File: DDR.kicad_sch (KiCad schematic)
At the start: 12 parts, among them U1 rv1126/rv1109, U2 Micron DDR4 MT40A512M16TB

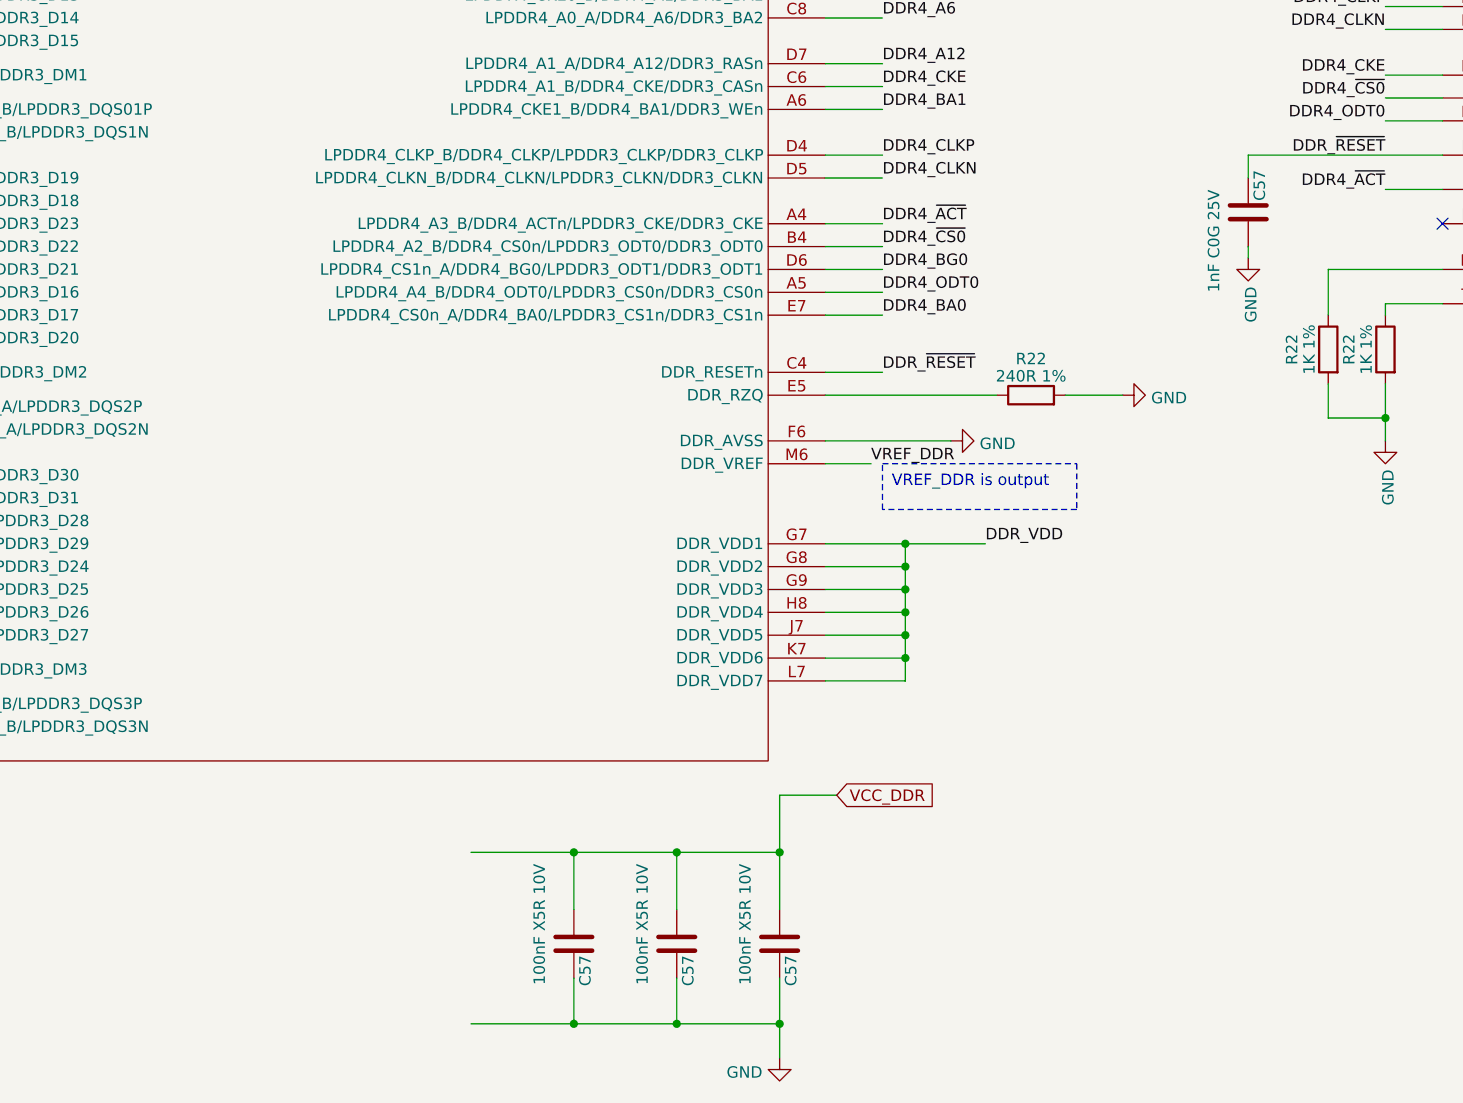
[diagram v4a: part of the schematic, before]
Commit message: updated Capacitors
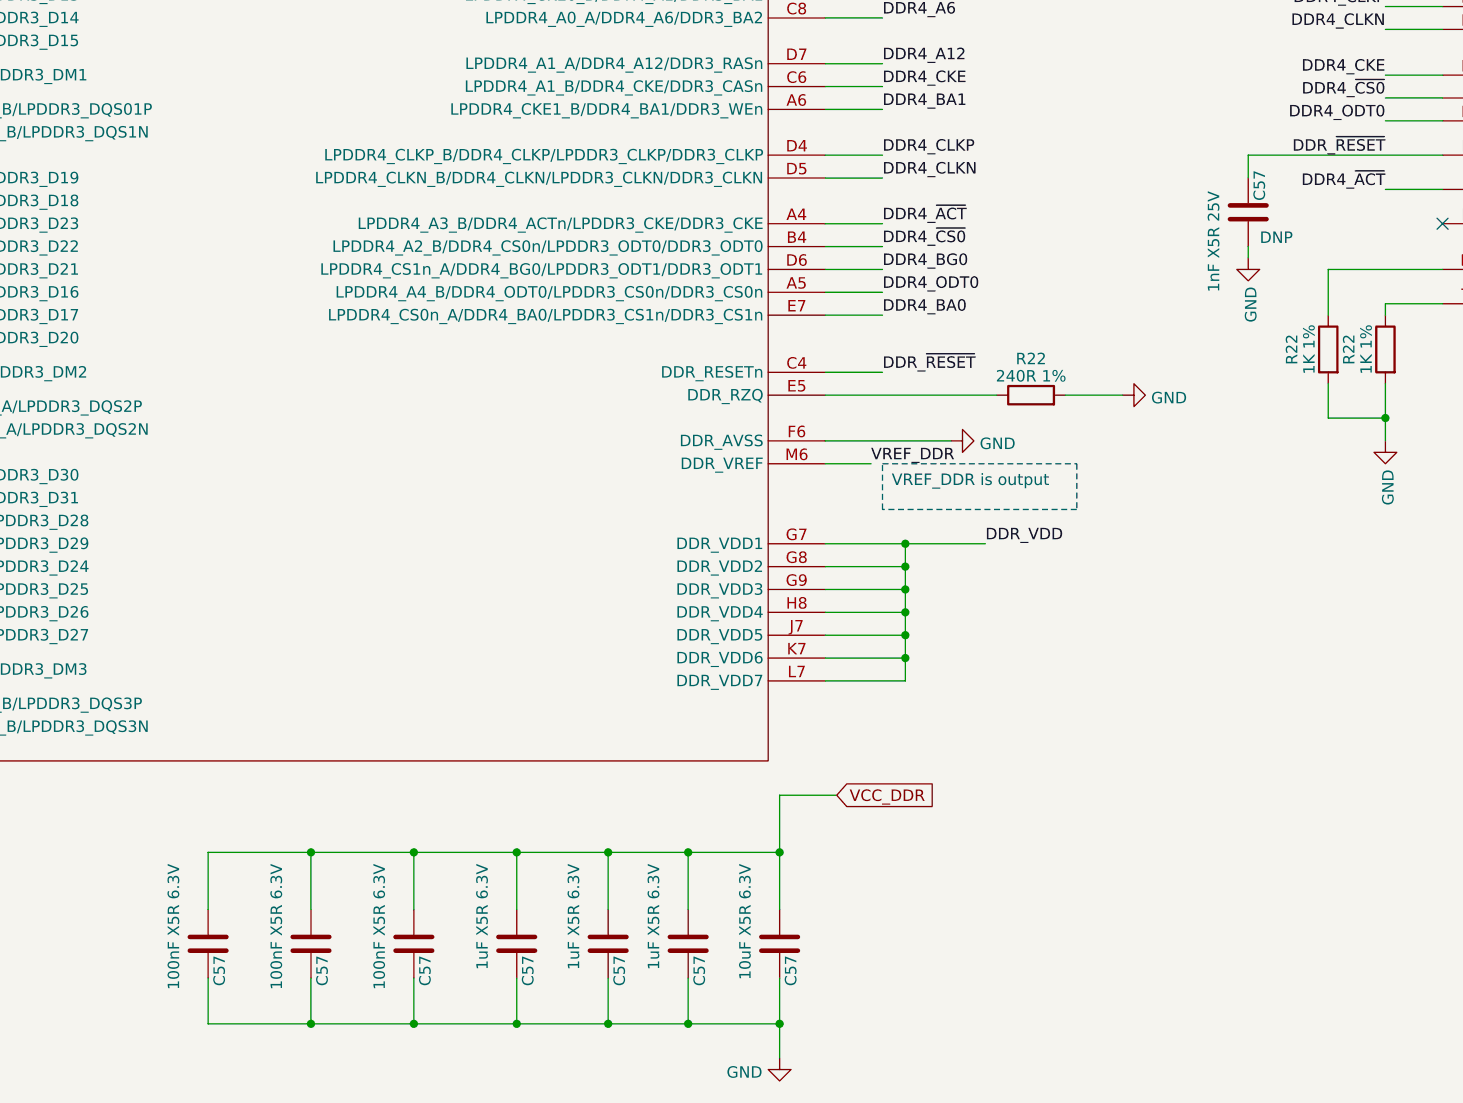
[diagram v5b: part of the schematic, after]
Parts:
- added C57 (x3): 1uF X5R 6.3V, Capacitor_SMD:C_0201_0603Metric, symbol Device:C
- added C57: 10uF X5R 6.3V, Capacitor_SMD:C_0603_1608Metric, symbol Device:C
- C57: footprint Capacitor_SMD:C_0402_1005Metric -> Capacitor_SMD:C_0201_0603Metric; now left out of the parts list
- C57: value 1nF C0G 25V -> 1nF X5R 25V; footprint Capacitor_SMD:C_0402_1005Metric -> Capacitor_SMD:C_0201_0603Metric; LCSC (none) -> C161477; Model (none) -> GRM033R61E102KA01D; Vendor (none) -> muRata(村田); now left out of the parts list
- C57: value 100nF X5R 10V -> 100nF X5R 6.3V; footprint Capacitor_SMD:C_0402_1005Metric -> Capacitor_SMD:C_0201_0603Metric; LCSC (none) -> C76934; Model (none) -> GRM033R61A104KE15D; Vendor (none) -> muRata(村田)
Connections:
- net GND: now also C57.1, C57.1, C57.1, C57.1
- net VCC_DDR: now also C57.2, C57.2, C57.2, C57.2
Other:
- moved on the sheet: C57

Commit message: updated LCSC selection of capacitors
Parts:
- C57: footprint Capacitor_SMD:C_0603_1608Metric -> Capacitor_SMD:C_0402_1005Metric; LCSC (none) -> C77000; Model (none) -> GRM155R61A106ME44D; Vendor (none) -> muRata(村田)
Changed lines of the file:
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@@
       (effects (font (size 1.27 1.27)) (justify left))
     )
-    (property "Footprint" "Capacitor_SMD:C_0603_1608Metric" (at 154.6352 176.53 0)
+    (property "Footprint" "Capacitor_SMD:C_0402_1005Metric" (at 154.6352 176.53 0)
       (effects (font (size 1.27 1.27)) hide)
     )
@@
       (effects (font (size 1.27 1.27)) hide)
     )
+    (property "Description" "容值: 10uF 精度: ±20% 额定电压: 10V 材质(温度系数): X5R 材质:X5R" (at 153.67 180.34 0)
+      (effects (font (size 1.27 1.27)) hide)
+    )
+    (property "LCSC" "C77000" (at 153.67 180.34 0)
+      (effects (font (size 1.27 1.27)) hide)
+    )
+    (property "Model" "GRM155R61A106ME44D" (at 153.67 180.34 0)
+      (effects (font (size 1.27 1.27)) hide)
+    )
+    (property "Vendor" "muRata(村田)" (at 153.67 180.34 0)
+      (effects (font (size 1.27 1.27)) hide)
+    )

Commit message: updated DDR_VDD
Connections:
- net DDR_VDD is gone; now on net VCC_DDR: U1.G7 (DDR_VDD1), U1.G8 (DDR_VDD2), U1.G9 (DDR_VDD3), U1.H8 (DDR_VDD4), U1.J7 (DDR_VDD5), U1.K7 (DDR_VDD6), U1.L7 (DDR_VDD7)
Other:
- moved on the sheet: C57, R22

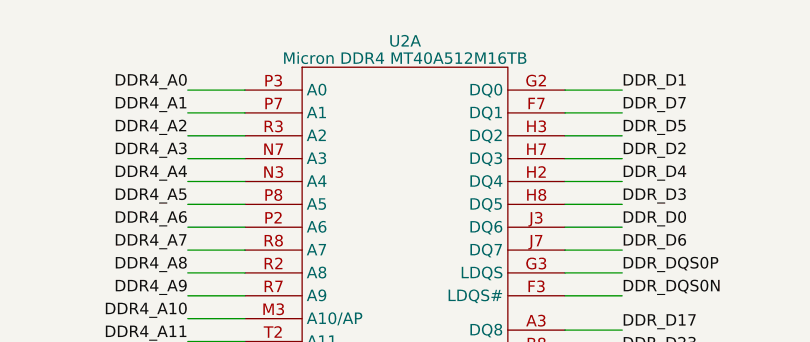
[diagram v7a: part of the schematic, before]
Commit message: layout SoC Power and DDR capacitors
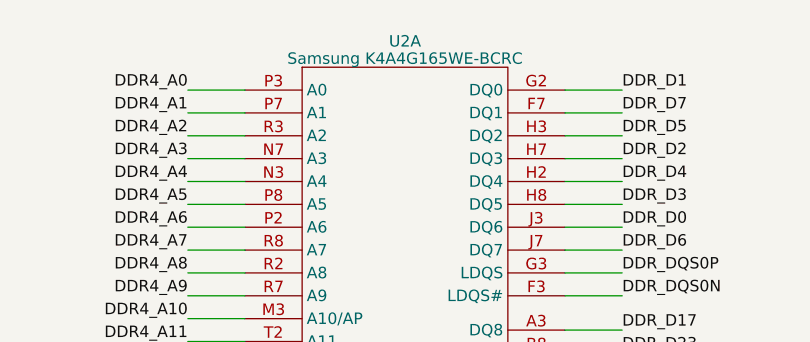
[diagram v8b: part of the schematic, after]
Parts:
- C57: LCSC C76934 -> C76928; Model GRM033R61A104KE15D -> GRM033R60J104KE19D
- C57: footprint Capacitor_SMD:C_0201_0603Metric -> Capacitor_SMD:C_0402_1005Metric; LCSC C76929 -> C15684; Model GRM033R60J105KEA2D -> GRM155R60J105KE19D
- U2: value Micron DDR4 MT40A512M16TB -> Samsung K4A4G165WE-BCRC; footprint (none) -> Package_BGA:Micron_FBGA-96_9x14mm_Layout9x16_P0.8mm; LCSC (none) -> C2803250; Model (none) -> K4A4G165WE-BCRC; Vendor (none) -> SAMSUNG(三星半导体)
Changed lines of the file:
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@@
       (effects (font (size 1.27 1.27)))
     )
-    (property "Value" "Micron DDR4 MT40A512M16TB" (at 245.11 25.7081 0)
-      (effects (font (size 1.27 1.27)))
-    )
-    (property "Footprint" "" (at 245.11 64.77 0)
+    (property "Value" "Samsung K4A4G165WE-BCRC" (at 245.11 25.7081 0)
+      (effects (font (size 1.27 1.27)))
+    )
+    (property "Footprint" "Package_BGA:Micron_FBGA-96_9x14mm_Layout9x16_P0.8mm" (at 245.11 64.77 0)
       (effects (font (size 1.27 1.27)) hide)
     )
     (property "Datasheet" "" (at 245.11 64.77 0)
+      (effects (font (size 1.27 1.27)) hide)
+    )
+    (property "Description" "存储器构架(格式): SDRAM DDR4 时钟频率(fc): 1200MHz 存储容量: 4Gbit 工作电压: 1.14V~1.26V 工作电" (at 245.11 64.77 0)
+      (effects (font (size 1.27 1.27)) hide)
+    )
+    (property "LCSC" "C2803250" (at 245.11 64.77 0)
+      (effects (font (size 1.27 1.27)) hide)
+    )
+    (property "Model" "K4A4G165WE-BCRC" (at 245.11 64.77 0)
+      (effects (font (size 1.27 1.27)) hide)
+    )
+    (property "Vendor" "SAMSUNG(三星半导体)" (at 245.11 64.77 0)
       (effects (font (size 1.27 1.27)) hide)
     )
@@
       (effects (font (size 1.27 1.27)) hide)
     )
-    (property "Description" "容值: 100nF 精度: ±10% 额定电压: 10V 材质(温度系数): X5R 材质:X5R" (at 138.43 180.34 0)
-      (effects (font (size 1.27 1.27)) hide)
-    )
-    (property "LCSC" "C76934" (at 138.43 180.34 0)
-      (effects (font (size 1.27 1.27)) hide)
-    )
-    (property "Model" "GRM033R61A104KE15D" (at 138.43 180.34 0)
+    (property "Description" "容值: 100nF 精度: ±10% 额定电压: 6.3V 材质(温度系数): X5R 材质:X5R" (at 138.43 180.34 0)
+      (effects (font (size 1.27 1.27)) hide)
+    )
+    (property "LCSC" "C76928" (at 138.43 180.34 0)
+      (effects (font (size 1.27 1.27)) hide)
+    )
+    (property "Model" "GRM033R60J104KE19D" (at 138.43 180.34 0)
       (effects (font (size 1.27 1.27)) hide)
     )
@@
       (effects (font (size 1.27 1.27)) (justify left))
     )
-    (property "Footprint" "Capacitor_SMD:C_0201_0603Metric" (at 115.8748 176.53 0)
+    (property "Footprint" "Capacitor_SMD:C_0402_1005Metric" (at 115.8748 176.53 0)
       (effects (font (size 1.27 1.27)) hide)
     )
@@
       (effects (font (size 1.27 1.27)) hide)
     )
-    (property "LCSC" "C76929" (at 116.84 180.34 0)
-      (effects (font (size 1.27 1.27)) hide)
-    )
-    (property "Model" "GRM033R60J105KEA2D" (at 116.84 180.34 0)
+    (property "LCSC" "C15684" (at 116.84 180.34 0)
+      (effects (font (size 1.27 1.27)) hide)
+    )
+    (property "Model" "GRM155R60J105KE19D" (at 116.84 180.34 0)
       (effects (font (size 1.27 1.27)) hide)
     )
@@
       (effects (font (size 1.27 1.27)) (justify left))
     )
-    (property "Footprint" "Capacitor_SMD:C_0201_0603Metric" (at 106.9848 176.53 0)
+    (property "Footprint" "Capacitor_SMD:C_0402_1005Metric" (at 106.9848 176.53 0)
       (effects (font (size 1.27 1.27)) hide)
     )
@@
       (effects (font (size 1.27 1.27)) hide)
     )
-    (property "LCSC" "C76929" (at 107.95 180.34 0)
-      (effects (font (size 1.27 1.27)) hide)
-    )
-    (property "Model" "GRM033R60J105KEA2D" (at 107.95 180.34 0)
+    (property "LCSC" "C15684" (at 107.95 180.34 0)
+      (effects (font (size 1.27 1.27)) hide)
+    )
+    (property "Model" "GRM155R60J105KE19D" (at 107.95 180.34 0)
       (effects (font (size 1.27 1.27)) hide)
     )
@@
       (effects (font (size 1.27 1.27)) hide)
     )
-    (property "Description" "容值: 100nF 精度: ±10% 额定电压: 10V 材质(温度系数): X5R 材质:X5R" (at 149.86 180.34 0)
-      (effects (font (size 1.27 1.27)) hide)
-    )
-    (property "LCSC" "C76934" (at 149.86 180.34 0)
-      (effects (font (size 1.27 1.27)) hide)
-    )
-    (property "Model" "GRM033R61A104KE15D" (at 149.86 180.34 0)
+    (property "Description" "容值: 100nF 精度: ±10% 额定电压: 6.3V 材质(温度系数): X5R 材质:X5R" (at 149.86 180.34 0)
+      (effects (font (size 1.27 1.27)) hide)
+    )
+    (property "LCSC" "C76928" (at 149.86 180.34 0)
+      (effects (font (size 1.27 1.27)) hide)
+    )
+    (property "Model" "GRM033R60J104KE19D" (at 149.86 180.34 0)
       (effects (font (size 1.27 1.27)) hide)
     )
@@
       (effects (font (size 1.27 1.27)) (justify left))
     )
-    (property "Footprint" "Capacitor_SMD:C_0201_0603Metric" (at 126.0348 176.53 0)
+    (property "Footprint" "Capacitor_SMD:C_0402_1005Metric" (at 126.0348 176.53 0)
       (effects (font (size 1.27 1.27)) hide)
     )
@@
       (effects (font (size 1.27 1.27)) hide)
     )
-    (property "LCSC" "C76929" (at 127 180.34 0)
-      (effects (font (size 1.27 1.27)) hide)
-    )
-    (property "Model" "GRM033R60J105KEA2D" (at 127 180.34 0)
+    (property "LCSC" "C15684" (at 127 180.34 0)
+      (effects (font (size 1.27 1.27)) hide)
+    )
+    (property "Model" "GRM155R60J105KE19D" (at 127 180.34 0)
       (effects (font (size 1.27 1.27)) hide)
     )
@@
       (effects (font (size 1.27 1.27)) hide)
     )
-    (property "LCSC" "C76934" (at 161.29 180.34 90)
-      (effects (font (size 1.27 1.27)) hide)
-    )
-    (property "Description" "容值: 100nF 精度: ±10% 额定电压: 10V 材质(温度系数): X5R 材质:X5R" (at 161.29 180.34 90)
-      (effects (font (size 1.27 1.27)) hide)
-    )
-    (property "Model" "GRM033R61A104KE15D" (at 161.29 180.34 0)
-      (effects (font (size 1.27 1.27)) hide)
-    )
+    (property "LCSC" "C76928" (at 161.29 180.34 90)
+      (effects (font (size 1.27 1.27)) hide)
+    )
+    (property "Description" "容值: 100nF 精度: ±10% 额定电压: 6.3V 材质(温度系数): X5R 材质:X5R" (at 161.29 180.34 90)
+      (effects (font (size 1.27 1.27)) hide)
+    )
+    (property "Model" "GRM033R60J104KE19D" (at 161.29 180.34 0)
+      (effects (font (size 1.27 1.27)) hide)
+    )
